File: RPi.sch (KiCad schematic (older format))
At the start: 8 parts, among them U3 LMS6002DR2, U4 ECP5, X3 RaspberryPiConnector

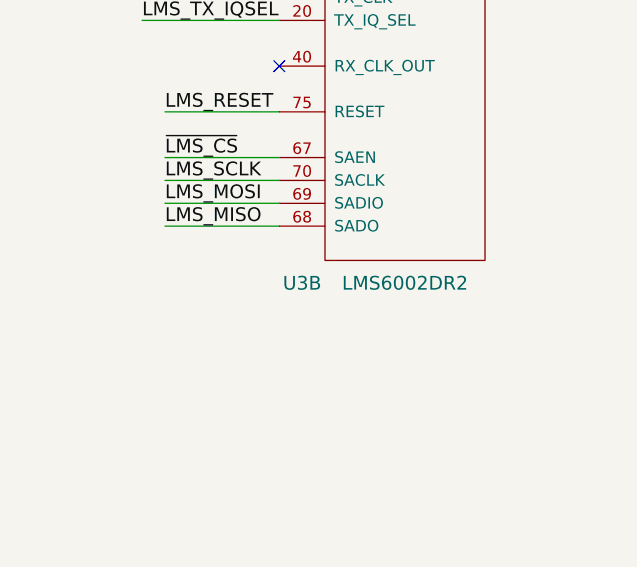
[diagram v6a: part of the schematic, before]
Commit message: Prepared BOM and changed some part numbers for unpopular ones. Added manufacture PN for each part.
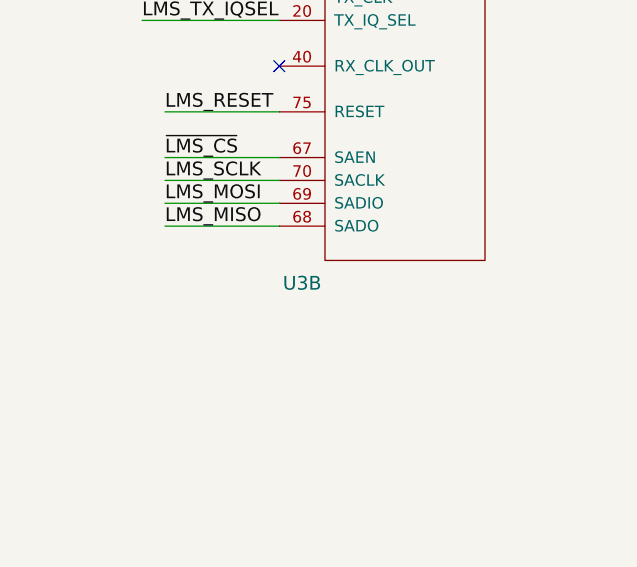
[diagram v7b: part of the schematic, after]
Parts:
- D3: manf# (none) -> 5512509F
- D4: manf# (none) -> 5510209F
- R8: manf# (none) -> RC0603JR-070RL
- U3: Component Value LMS6002DR2 -> (none); Manufacturer Part Number LMS6002DFN -> (none); Vendor Digi-Key -> (none); Vendor Part Number 1434-1000-1-ND -> (none); manf# (none) -> LMS6002DFN
- U4: manf# (none) -> LFE5U-25F-6BG381I
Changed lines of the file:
@@
 LIBS:valves
 LIBS:sdr
-LIBS:usb-type-c
 LIBS:sdr-cache
 EELAYER 25 0
@@
 F 2 "Resistors_SMD:R_0603" V 1080 1350 50  0001 C CNN
 F 3 "" H 1150 1350 50  0000 C CNN
+F 4 "RC0603JR-070RL" H 1150 1350 60  0001 C CNN "manf#"
 	1    1150 1350
 	0    1    1    0
@@
 F 2 "sdr-foots:ECP5_381" H 4150 3050 60  0001 C CNN
 F 3 "" H 4150 3050 60  0001 C CNN
+F 4 "LFE5U-25F-6BG381I" H 5700 2500 60  0001 C CNN "manf#"
 	8    5700 2500
 	1    0    0    -1
@@
 F 2 "sdr-foots:ECP5_381" H 7350 2950 60  0001 C CNN
 F 3 "" H 7350 2950 60  0001 C CNN
+F 4 "LFE5U-25F-6BG381I" H 8900 2400 60  0001 C CNN "manf#"
 	9    8900 2400
 	1    0    0    -1
@@
 F 2 "sdr-foots:ECP5_381" H 3800 7850 60  0001 C CNN
 F 3 "" H 3800 7850 60  0001 C CNN
+F 4 "LFE5U-25F-6BG381I" H 5350 7300 60  0001 C CNN "manf#"
 	6    5350 7300
 	1    0    0    -1
@@
 F 2 "sdr-foots:ECP5_381" H 4150 5100 60  0001 C CNN
 F 3 "" H 4150 5100 60  0001 C CNN
+F 4 "LFE5U-25F-6BG381I" H 5700 4550 60  0001 C CNN "manf#"
 	7    5700 4550
 	1    0    0    -1
@@
 F 2 "sdr-foots:DQFN-120_via_off_pad" H 9160 5400 60  0001 C CNN
 F 3 "" H 9350 10150 60  0000 C CNN
-F 4 "1434-1000-1-ND" H 9140 5910 60  0001 C CNN "Vendor Part Number"
-F 5 "Digi-Key" H 9130 5820 60  0001 C CNN "Vendor"
-F 6 "IC, MULTI-FUNCTION, TRANSCEIVER," H 9130 5490 60  0001 C CNN "Description"
-F 7 "Lime Microsystems Ltd" H 9140 5720 60  0001 C CNN "Manufacturer"
-F 8 "LMS6002DFN" H 9130 5600 60  0001 C CNN "Manufacturer Part Number"
-F 9 "LMS6002DR2" H 9650 6100 60  0000 C CNN "Component Value"
+F 4 "LMS6002DFN" H 9300 6200 60  0001 C CNN "manf#"
+F 5 "IC, MULTI-FUNCTION, TRANSCEIVER," H 9130 5490 60  0001 C CNN "Description"
+F 6 "Lime Microsystems Ltd" H 9140 5720 60  0001 C CNN "Manufacturer"
 	2    9300 6200
 	1    0    0    -1
@@
 F 2 "sdr-foots:LED_IND_SINGLE" H 8000 3350 50  0001 C CNN
 F 3 "" H 8000 3350 50  0001 C CNN
+F 4 "5510209F" H 8000 3350 60  0001 C CNN "manf#"
 	1    8000 3350
 	-1   0    0    1
@@
 F 2 "sdr-foots:LED_IND_SINGLE" H 7550 6200 50  0001 C CNN
 F 3 "" H 7550 6200 50  0001 C CNN
+F 4 "5512509F" H 7550 6200 60  0001 C CNN "manf#"
 	1    7550 6200
 	-1   0    0    1
@@
 F 2 "sdr-foots:ECP5_381" H 1850 5800 60  0001 C CNN
 F 3 "" H 1850 5800 60  0001 C CNN
+F 4 "LFE5U-25F-6BG381I" H 3400 5250 60  0001 C CNN "manf#"
 	10   3400 5250
 	1    0    0    -1
